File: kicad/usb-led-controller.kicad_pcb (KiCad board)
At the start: 4 copper layers, 70 x 50 mm, 82 parts, among them J1 SWD, J2 PWR, J3 USB, J4 PWM_0, J5 PWM_1, J6 WS2812_0, J7 WS2812_1, Q1 NVS4409N, Q2 NVS4409N, Q3 NVS4409N, Q4 NVS4409N, Q5 NVS4409N, Q6 NVS4409N, U1 SN74LV1T125, U2 SN74LV1T125, U3 STM32F042F6Px, U4 MIC5501-XYM5, U5 USBLC6, U6 SN74LVC1G04

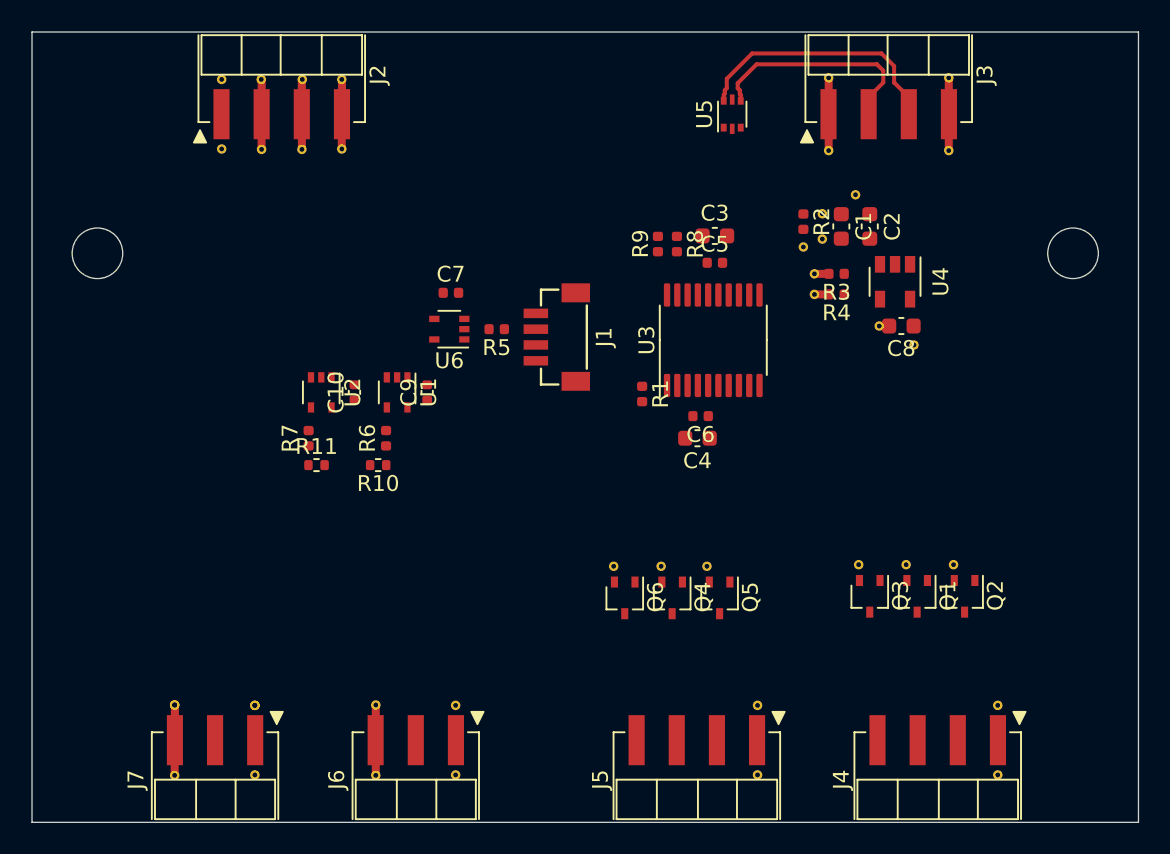
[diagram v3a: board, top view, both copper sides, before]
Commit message: Added polyfuses and reduced board size
This is much more reasonable. No need to take up all that space.
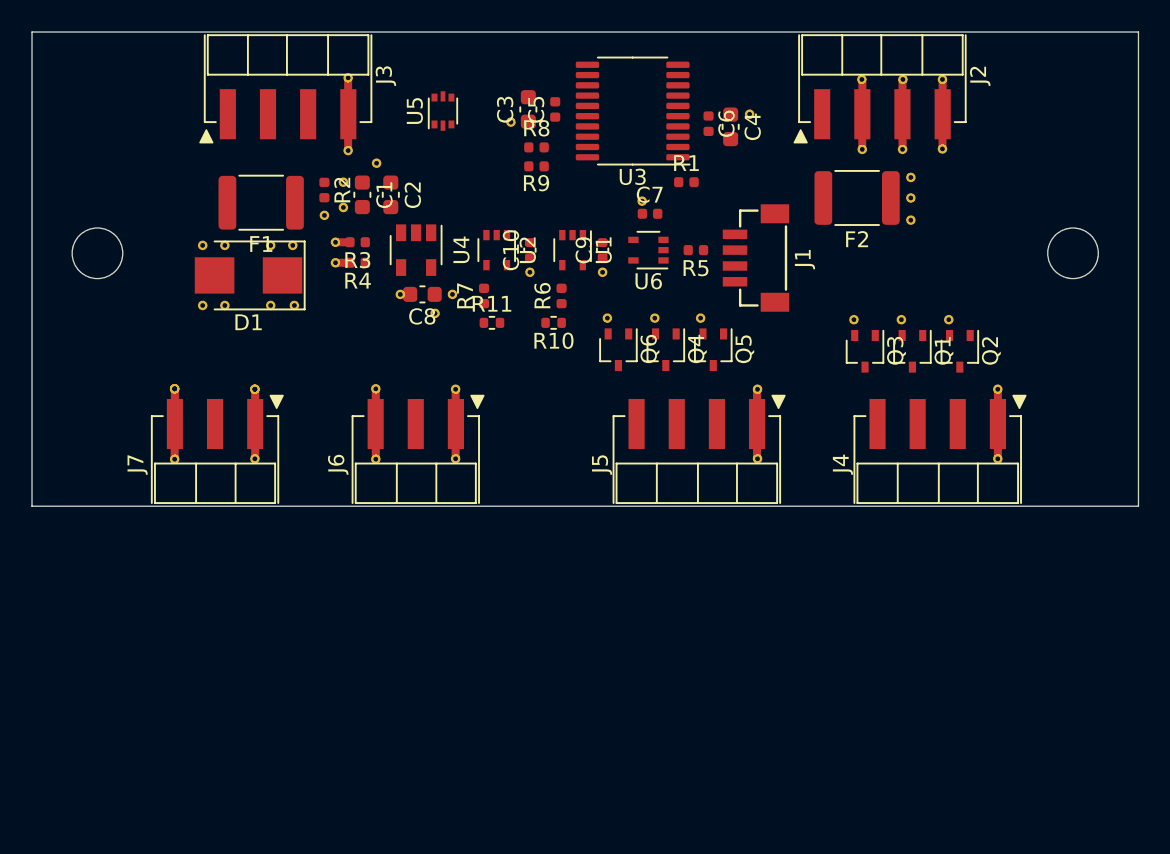
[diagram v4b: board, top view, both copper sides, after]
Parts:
- removed the REF** at (188.3, 133.7)
- removed the REF** at (156.8, 147.0)
- removed the REF** at (156.8, 142.6)
- removed the REF** at (191.1, 147.0)
- removed the REF** at (191.1, 142.6)
- removed the REF** at (175.9, 147.0)
- removed the REF** at (175.9, 142.6)
- removed the REF** at (185.8, 119.8)
- removed the REF** at (182.1, 110.3)
- removed the REF** at (185.3, 133.7)
- removed the REF** at (180.0, 111.5)
- removed the REF** at (183.6, 118.6)
- removed the REF** at (180.0, 113.1)
- removed the REF** at (178.8, 113.6)
- removed the REF** at (182.3, 133.7)
- removed the REF** at (139.0, 142.6) (x2)
- removed the REF** at (139.0, 147.0)
- removed the REF** at (151.8, 147.0)
- removed the REF** at (151.8, 142.6)
- removed the REF** at (179.5, 116.6)
- removed the REF** at (179.5, 115.3)
- removed the REF** at (188.0, 107.5)
- removed the REF** at (188.0, 102.9)
- removed the REF** at (180.4, 102.9)
- removed the REF** at (172.7, 133.8)
- removed the REF** at (180.4, 107.5)
- removed the REF** at (169.8, 133.8)
- removed the REF** at (166.8, 133.8)
- removed the REF** at (144.1, 142.6) (x2)
- removed the REF** at (144.1, 147.0)
- added D1: 3SMBJ5919B, Diode_SMD:D_SMB, F.Cu at (143.7, 115.4)
- added F1: Polyfuse, Resistor_SMD:R_1812_4532Metric, F.Cu at (144.5, 110.8)
- added F2: Polyfuse, Resistor_SMD:R_1812_4532Metric, F.Cu at (182.2, 110.5)
- added REF**: VIA-0.3_0.6-TENT, usb-led-controller:VIA-0.3_0.6-TENT, F.Cu at (161.5, 115.2)
- added REF**: VIA-0.3_0.6-TENT, usb-led-controller:VIA-0.3_0.6-TENT, F.Cu at (146.6, 117.3)
- added REF**: VIA-0.3_0.6-TENT, usb-led-controller:VIA-0.3_0.6-TENT, F.Cu at (145.1, 117.3)
- added REF**: VIA-0.3_0.6-TENT, usb-led-controller:VIA-0.3_0.6-TENT, F.Cu at (140.8, 113.5)
- added REF**: VIA-0.3_0.6-TENT, usb-led-controller:VIA-0.3_0.6-TENT, F.Cu at (142.2, 113.5)
- added REF**: VIA-0.3_0.6-TENT, usb-led-controller:VIA-0.3_0.6-TENT, F.Cu at (142.2, 117.3)
- added REF**: VIA-0.3_0.6-TENT, usb-led-controller:VIA-0.3_0.6-TENT, F.Cu at (140.8, 117.3)
- added REF**: VIA-0.3_0.6-TENT, usb-led-controller:VIA-0.3_0.6-TENT, F.Cu at (188.0, 118.2)
- added REF**: VIA-0.3_0.6-TENT, usb-led-controller:VIA-0.3_0.6-TENT, F.Cu at (185.0, 118.2)
- added REF**: VIA-0.3_0.6-TENT, usb-led-controller:VIA-0.3_0.6-TENT, F.Cu at (182.0, 118.2)
- added REF**: VIA-0.3_0.6-TENT, usb-led-controller:VIA-0.3_0.6-TENT, F.Cu at (172.3, 118.1)
- added REF**: VIA-0.3_0.6-TENT, usb-led-controller:VIA-0.3_0.6-TENT, F.Cu at (166.1, 115.2)
- added REF**: VIA-0.3_0.6-TENT, usb-led-controller:VIA-0.3_0.6-TENT, F.Cu at (169.4, 118.1)
- added REF**: VIA-0.3_0.6-TENT, usb-led-controller:VIA-0.3_0.6-TENT, F.Cu at (166.4, 118.1)
- added REF** (x2): VIA-0.3_0.6-TENT, usb-led-controller:VIA-0.3_0.6-TENT, F.Cu at (144.1, 122.6)
- added REF**: VIA-0.3_0.6-TENT, usb-led-controller:VIA-0.3_0.6-TENT, F.Cu at (144.1, 127.0)
- added REF**: VIA-0.3_0.6-TENT, usb-led-controller:VIA-0.3_0.6-TENT, F.Cu at (156.8, 127.0)
- added REF**: VIA-0.3_0.6-TENT, usb-led-controller:VIA-0.3_0.6-TENT, F.Cu at (156.8, 122.6)
- added REF**: VIA-0.3_0.6-TENT, usb-led-controller:VIA-0.3_0.6-TENT, F.Cu at (191.1, 127.0)
- added REF**: VIA-0.3_0.6-TENT, usb-led-controller:VIA-0.3_0.6-TENT, F.Cu at (191.1, 122.6)
- added REF**: VIA-0.3_0.6-TENT, usb-led-controller:VIA-0.3_0.6-TENT, F.Cu at (175.9, 127.0)
- added REF**: VIA-0.3_0.6-TENT, usb-led-controller:VIA-0.3_0.6-TENT, F.Cu at (156.6, 116.6)
- added REF**: VIA-0.3_0.6-TENT, usb-led-controller:VIA-0.3_0.6-TENT, F.Cu at (175.9, 122.6)
- added REF**: VIA-0.3_0.6-TENT, usb-led-controller:VIA-0.3_0.6-TENT, F.Cu at (155.5, 117.8)
- added REF**: VIA-0.3_0.6-TENT, usb-led-controller:VIA-0.3_0.6-TENT, F.Cu at (151.8, 108.3)
- added REF**: VIA-0.3_0.6-TENT, usb-led-controller:VIA-0.3_0.6-TENT, F.Cu at (149.7, 109.5)
- added REF**: VIA-0.3_0.6-TENT, usb-led-controller:VIA-0.3_0.6-TENT, F.Cu at (153.3, 116.6)
- added REF**: VIA-0.3_0.6-TENT, usb-led-controller:VIA-0.3_0.6-TENT, F.Cu at (149.7, 111.1)
- added REF**: VIA-0.3_0.6-TENT, usb-led-controller:VIA-0.3_0.6-TENT, F.Cu at (148.5, 111.6)
- added REF**: VIA-0.3_0.6-TENT, usb-led-controller:VIA-0.3_0.6-TENT, F.Cu at (168.6, 110.7)
- added REF** (x2): VIA-0.3_0.6-TENT, usb-led-controller:VIA-0.3_0.6-TENT, F.Cu at (139.0, 122.6)
- added REF**: VIA-0.3_0.6-TENT, usb-led-controller:VIA-0.3_0.6-TENT, F.Cu at (139.0, 127.0)
- added REF**: VIA-0.3_0.6-TENT, usb-led-controller:VIA-0.3_0.6-TENT, F.Cu at (151.8, 127.0)
- added REF**: VIA-0.3_0.6-TENT, usb-led-controller:VIA-0.3_0.6-TENT, F.Cu at (151.8, 122.6)
- added REF**: VIA-0.3_0.6-TENT, usb-led-controller:VIA-0.3_0.6-TENT, F.Cu at (175.4, 105.2)
- added REF**: VIA-0.3_0.6-TENT, usb-led-controller:VIA-0.3_0.6-TENT, F.Cu at (149.2, 114.6)
- added REF**: VIA-0.3_0.6-TENT, usb-led-controller:VIA-0.3_0.6-TENT, F.Cu at (149.2, 113.3)
- added REF**: VIA-0.3_0.6-TENT, usb-led-controller:VIA-0.3_0.6-TENT, F.Cu at (150.0, 107.5)
- added REF**: VIA-0.3_0.6-TENT, usb-led-controller:VIA-0.3_0.6-TENT, F.Cu at (150.0, 102.9)
- added REF**: VIA-0.3_0.6-TENT, usb-led-controller:VIA-0.3_0.6-TENT, F.Cu at (160.3, 105.7)
- added REF**: VIA-0.3_0.6-TENT, usb-led-controller:VIA-0.3_0.6-TENT, F.Cu at (185.6, 111.9)
- added REF**: VIA-0.3_0.6-TENT, usb-led-controller:VIA-0.3_0.6-TENT, F.Cu at (145.1, 113.5)
- added REF**: VIA-0.3_0.6-TENT, usb-led-controller:VIA-0.3_0.6-TENT, F.Cu at (146.5, 113.5)
- moved REF** 44.2 mm to (185.6, 110.5)
- moved REF** 43.6 mm to (185.6, 109.2)
- moved J2 38.0 mm to (183.8, 105.2)
- moved J3 38.0 mm to (146.2, 105.2)
- moved REF** 38.0 mm to (182.5, 103.0)
- moved REF** 38.0 mm to (185.1, 103.0)
- moved REF** 38.0 mm to (187.6, 103.0)
- moved REF** 38.0 mm to (187.6, 107.4)
- moved REF** 38.0 mm to (185.1, 107.4)
- moved REF** 38.0 mm to (182.5, 107.4)
- moved C2 30.4 mm to (152.7, 110.3)
- moved C8 30.4 mm to (154.7, 116.6)
- moved R2 30.4 mm to (148.5, 110.0)
- moved R3 30.4 mm to (150.6, 113.3)
- moved R4 30.4 mm to (150.6, 114.6)
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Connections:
- J2 pad 1: +12V -> /+12V_RAW
- J3 pad 1: +5V -> /+5V_RAW
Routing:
- net /USB_D+: track 16.5 -> 0.00 mm
- net /USB_D-: track 14.2 -> 0.00 mm
- net +12V: track 0.00 -> 8.83 mm
- net +5V: track 5.52 -> 9.75 mm
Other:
- board size 70 x 50 mm -> 70 x 30 mm

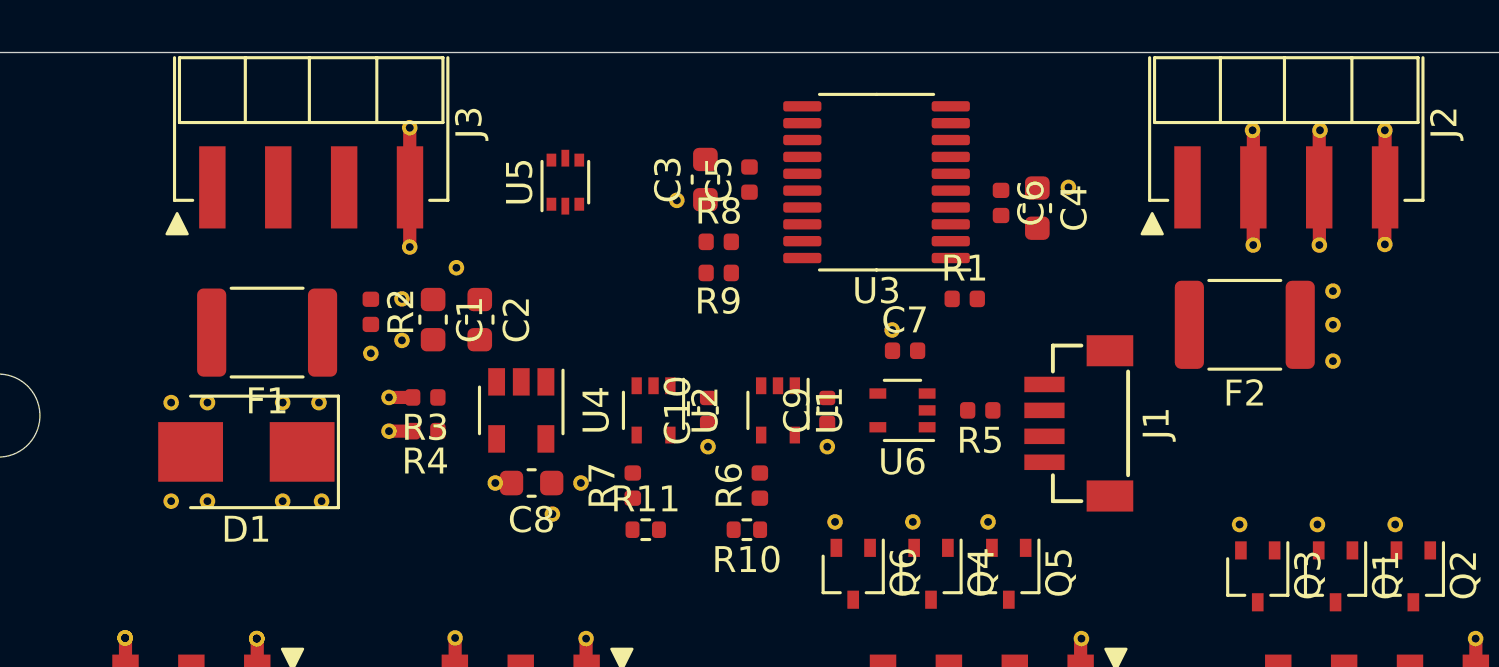
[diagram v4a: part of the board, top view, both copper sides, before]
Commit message: Added power planes to 3rd layer
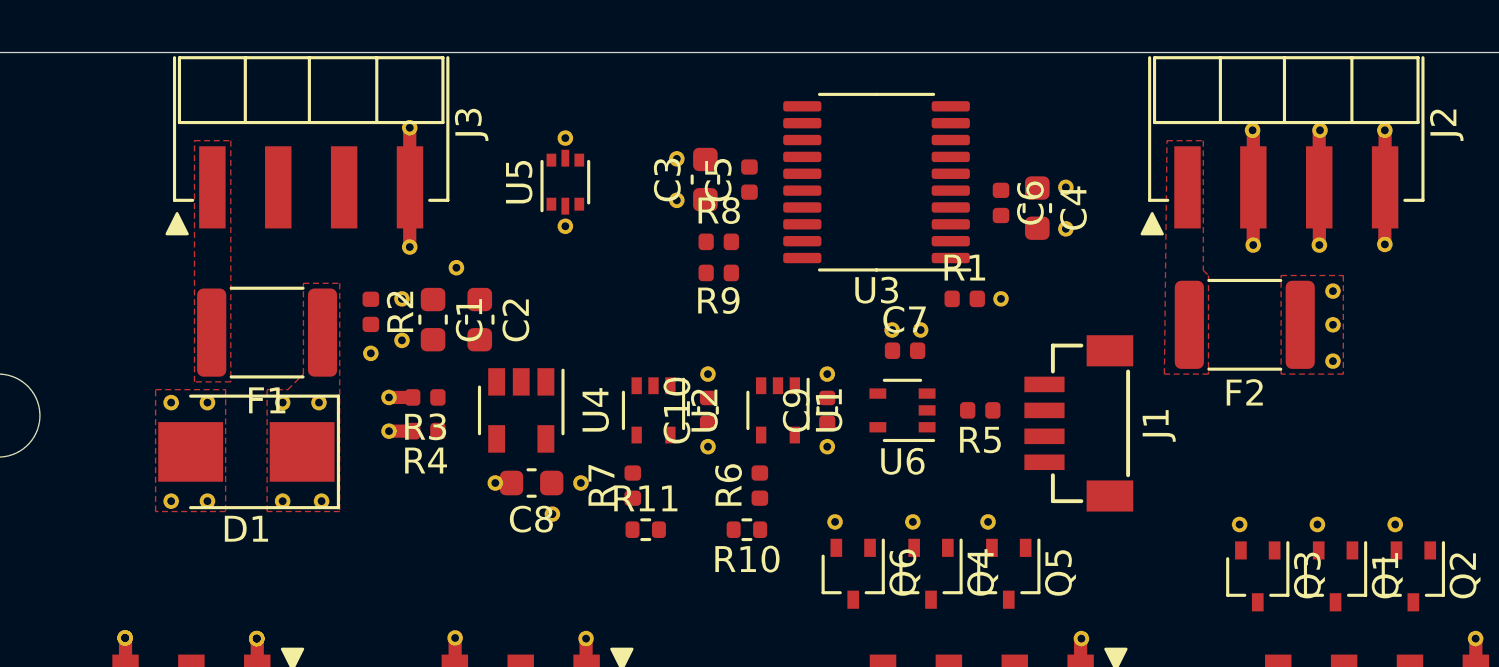
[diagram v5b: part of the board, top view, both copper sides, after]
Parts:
- added REF**: VIA-0.3_0.6-TENT, usb-led-controller:VIA-0.3_0.6-TENT, F.Cu at (161.5, 112.4)
- added REF**: VIA-0.3_0.6-TENT, usb-led-controller:VIA-0.3_0.6-TENT, F.Cu at (166.1, 112.4)
- added REF**: VIA-0.3_0.6-TENT, usb-led-controller:VIA-0.3_0.6-TENT, F.Cu at (169.7, 110.7)
- added REF**: VIA-0.3_0.6-TENT, usb-led-controller:VIA-0.3_0.6-TENT, F.Cu at (172.8, 109.5)
- added REF**: VIA-0.3_0.6-TENT, usb-led-controller:VIA-0.3_0.6-TENT, F.Cu at (175.3, 106.8)
- added REF**: VIA-0.3_0.6-TENT, usb-led-controller:VIA-0.3_0.6-TENT, F.Cu at (160.3, 104.1)
- added REF**: VIA-0.3_0.6-TENT, usb-led-controller:VIA-0.3_0.6-TENT, F.Cu at (156.0, 106.7)
- added REF**: VIA-0.3_0.6-TENT, usb-led-controller:VIA-0.3_0.6-TENT, F.Cu at (156.0, 103.3)
- moved REF** 0.10 mm to (175.3, 105.2)
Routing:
- added copper zone on F.Cu, net +12V
- added copper zone on In2.Cu, net +12V
- added copper zone on In2.Cu, net +3V3
- added copper zone on F.Cu, net +5V
- added copper zone on In2.Cu, net +5V
- added copper zone on F.Cu, net /+12V_RAW
- added copper zone on F.Cu, net /+5V_RAW
- added copper zone on F.Cu, net GND

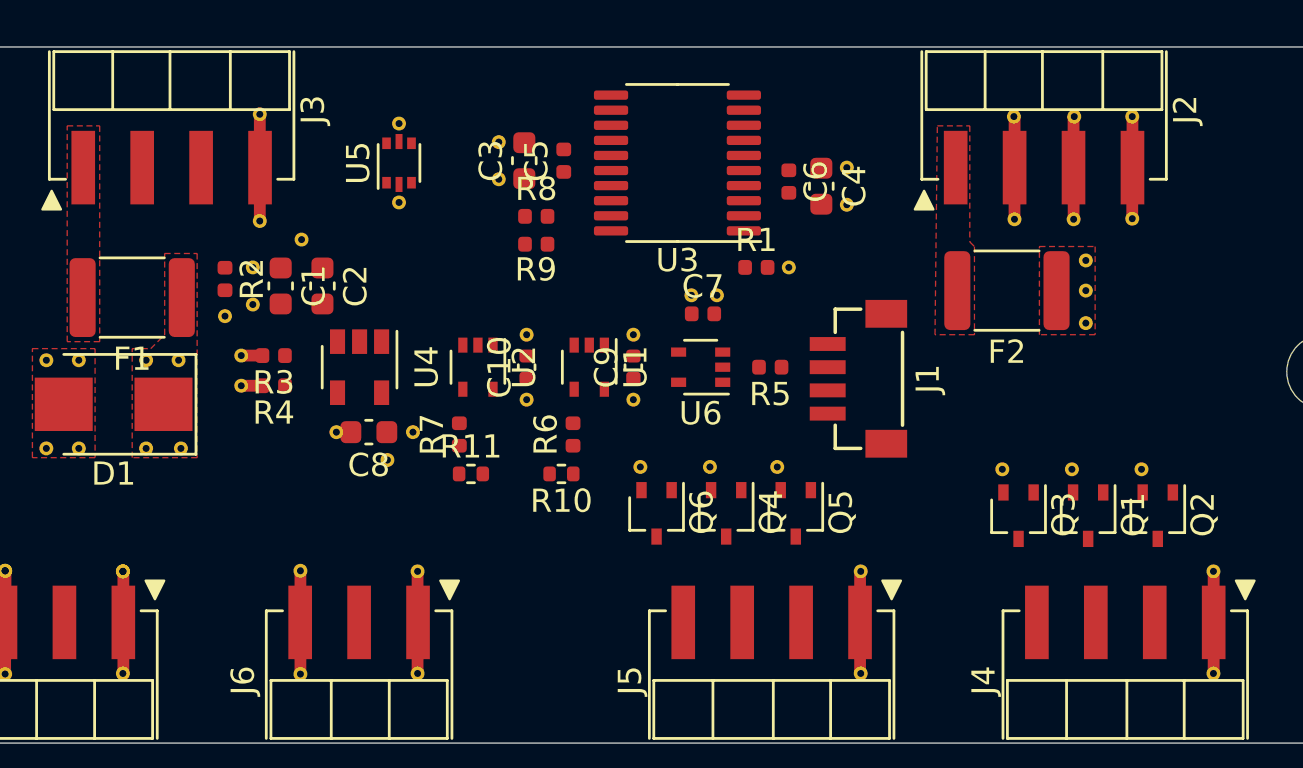
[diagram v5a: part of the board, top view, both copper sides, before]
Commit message: Added power planes on top layer and a few traces
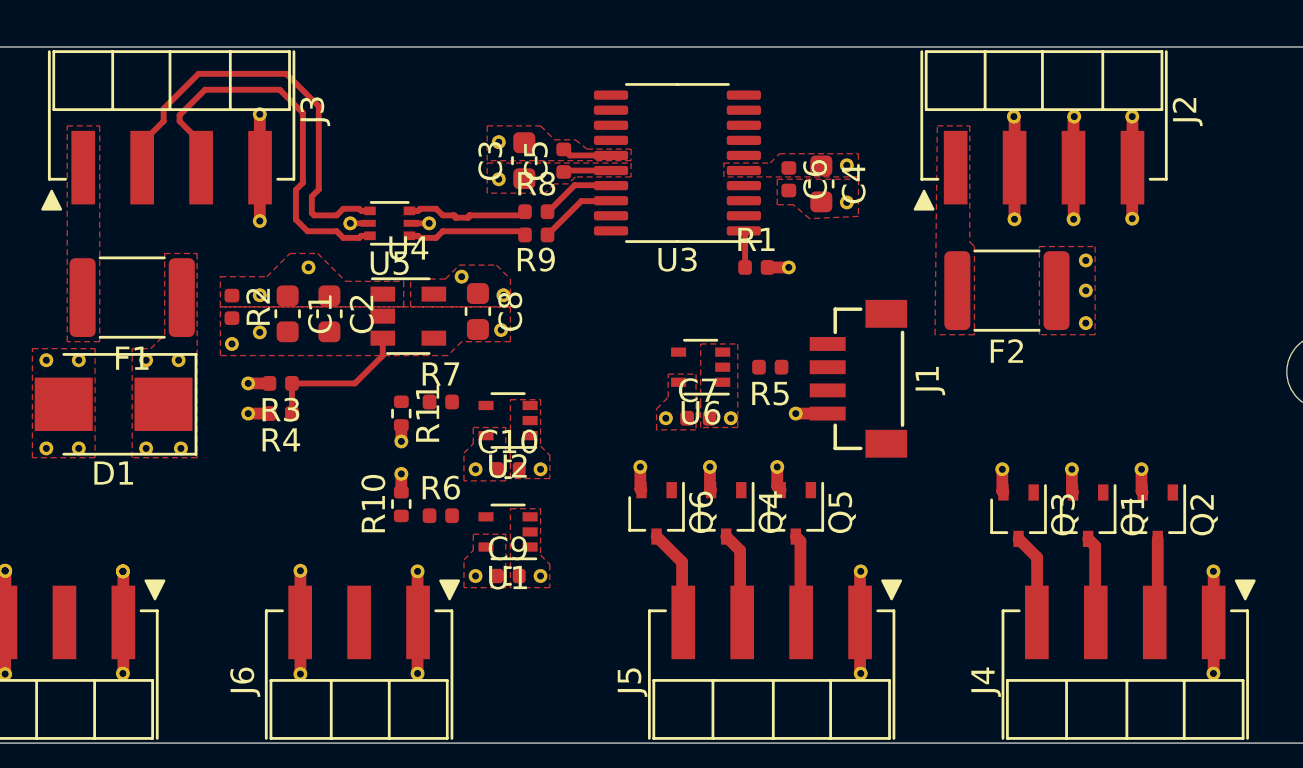
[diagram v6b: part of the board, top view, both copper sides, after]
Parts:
- added REF**: VIA-0.3_0.6-TENT, usb-led-controller:VIA-0.3_0.6-TENT, F.Cu at (173.1, 115.8)
- added REF**: VIA-0.3_0.6-TENT, usb-led-controller:VIA-0.3_0.6-TENT, F.Cu at (156.1, 117.0)
- added REF**: VIA-0.3_0.6-TENT, usb-led-controller:VIA-0.3_0.6-TENT, F.Cu at (156.1, 118.4)
- moved REF** 11.1 mm to (162.1, 122.8), turned to 270 degrees
- moved C9 10.5 mm to (160.7, 122.8), turned to 0 degrees
- moved REF** 10.2 mm to (159.3, 122.8), turned to 90 degrees
- moved REF** 8.52 mm to (158.7, 109.9)
- moved REF** 8.35 mm to (160.4, 112.2)
- moved U1 7.92 mm to (160.7, 120.9), turned to 180 degrees
- moved REF** 7.07 mm to (160.5, 110.7)
- moved R10 7.02 mm to (156.1, 119.7), turned to 90 degrees
- moved C8 7.01 mm to (159.4, 111.4), turned to 270 degrees
- moved R6 6.69 mm to (157.8, 120.2), turned to 0 degrees
- moved REF** 5.83 mm to (162.1, 118.2), turned to 270 degrees
- moved REF** 5.41 mm to (167.5, 116.0)
- moved REF** 5.33 mm to (170.3, 116.0)
- moved REF** 4.79 mm to (153.9, 107.6), turned to 90 degrees
- moved C7 4.50 mm to (168.9, 116.0)
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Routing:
- net /USB_D-: track 0.00 -> 18.2 mm
- net /USB_D+: track 0.00 -> 17.1 mm
- net GND: track 27.7 -> 40.6 mm
- net /REG_3V3_EN: track 0.00 -> 6.46 mm
- net /USB_D_TVS-: track 0.00 -> 5.31 mm
- net /USB_D_TVS+: track 0.00 -> 5.20 mm
- net /PWM_1_B: track 0.00 -> 4.18 mm
- net /PWM_1_R: track 0.00 -> 3.99 mm
- net /PWM_0_B: track 0.00 -> 3.94 mm
- net /PWM_1_G: track 0.00 -> 3.80 mm
- net /PWM_0_R: track 0.00 -> 3.74 mm
- net /PWM_0_G: track 0.00 -> 3.65 mm
- net /USB_D_R+: track 0.00 -> 3.35 mm
- net /USB_D_R-: track 0.00 -> 3.22 mm
- net +3V3: track 0.00 -> 2.06 mm
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- added copper zone on F.Cu, net +3V3
